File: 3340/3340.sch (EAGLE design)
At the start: 74 parts, among them IC2 CEM3340, Q1 2N3906, X1 2516-

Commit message: fixed the levels for the 3340 and vcf3
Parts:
- C6: value 1n -> 68p
- R30, R31: value 1k -> 100k
- R7, R8: value 22k -> 1k
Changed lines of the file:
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@@
 <part name="PWM" library="dan" deviceset="PJ301BM" device=""/>
 <part name="GND4" library="dan" deviceset="GND" device=""/>
-<part name="R8" library="dan" deviceset="R-US_" device="0207/7" value="22k"/>
+<part name="R8" library="dan" deviceset="R-US_" device="0207/7" value="1k"/>
 <part name="GND20" library="dan" deviceset="GND" device=""/>
 <part name="GND21" library="dan" deviceset="GND" device=""/>
@@
 <part name="C1" library="dan" deviceset="C-US" device="050-025X075" value="1n"/>
 <part name="GND5" library="dan" deviceset="GND" device=""/>
-<part name="R7" library="dan" deviceset="R-US_" device="0207/7" value="22k"/>
+<part name="R7" library="dan" deviceset="R-US_" device="0207/7" value="1k"/>
 <part name="HF" library="dan" deviceset="TRIM_US-" device="S64W" value="20k"/>
 <part name="GND11" library="dan" deviceset="GND" device=""/>
@@
 <part name="SYNC" library="dan" deviceset="PJ301BM" device=""/>
 <part name="GND6" library="dan" deviceset="GND" device=""/>
-<part name="C6" library="dan" deviceset="C-US" device="050-025X075" value="1n"/>
+<part name="C6" library="dan" deviceset="C-US" device="050-025X075" value="68p"/>
 <part name="GND9" library="dan" deviceset="GND" device=""/>
 <part name="P+4" library="dan" deviceset="+12V" device=""/>
@@
 <part name="P+6" library="dan" deviceset="+12V" device=""/>
 <part name="R29" library="dan" deviceset="R-US_" device="0207/7" value="10k"/>
-<part name="R30" library="dan" deviceset="R-US_" device="0207/7" value="1k"/>
-<part name="R31" library="dan" deviceset="R-US_" device="0207/7" value="1k"/>
+<part name="R30" library="dan" deviceset="R-US_" device="0207/7" value="100k"/>
+<part name="R31" library="dan" deviceset="R-US_" device="0207/7" value="100k"/>
 <part name="GND27" library="dan" deviceset="GND" device=""/>
 <part name="GND28" library="dan" deviceset="GND" device=""/>

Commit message: added state variable filter, changed pw resistor on vco
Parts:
- R29: value 10k -> 1k
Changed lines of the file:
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@@
 <part name="R28" library="dan" deviceset="R-US_" device="0207/7" value="10k"/>
 <part name="P+6" library="dan" deviceset="+12V" device=""/>
-<part name="R29" library="dan" deviceset="R-US_" device="0207/7" value="10k"/>
+<part name="R29" library="dan" deviceset="R-US_" device="0207/7" value="1k"/>
 <part name="R30" library="dan" deviceset="R-US_" device="0207/7" value="100k"/>
 <part name="R31" library="dan" deviceset="R-US_" device="0207/7" value="100k"/>

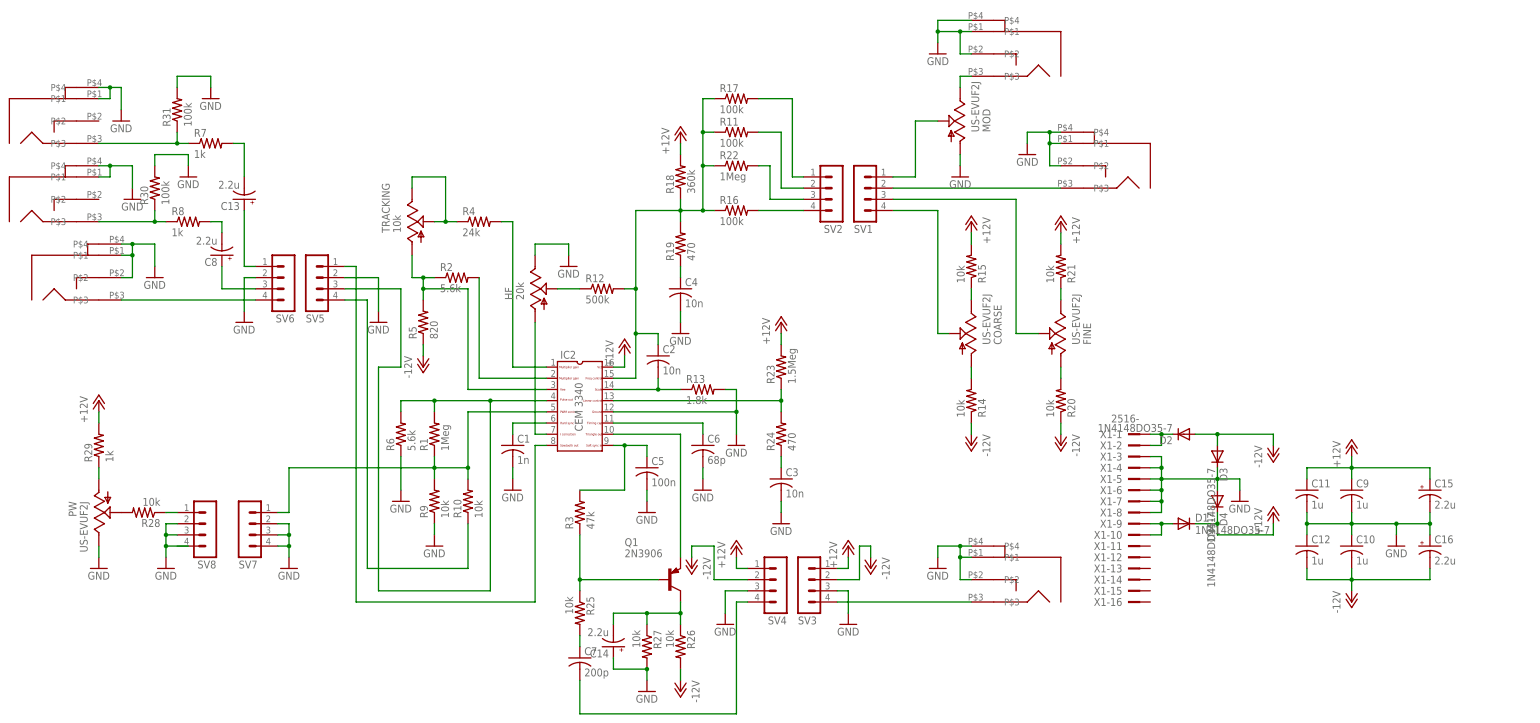
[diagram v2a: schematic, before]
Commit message: added tri and linear mod to vco, fixed serious errors with cvsource
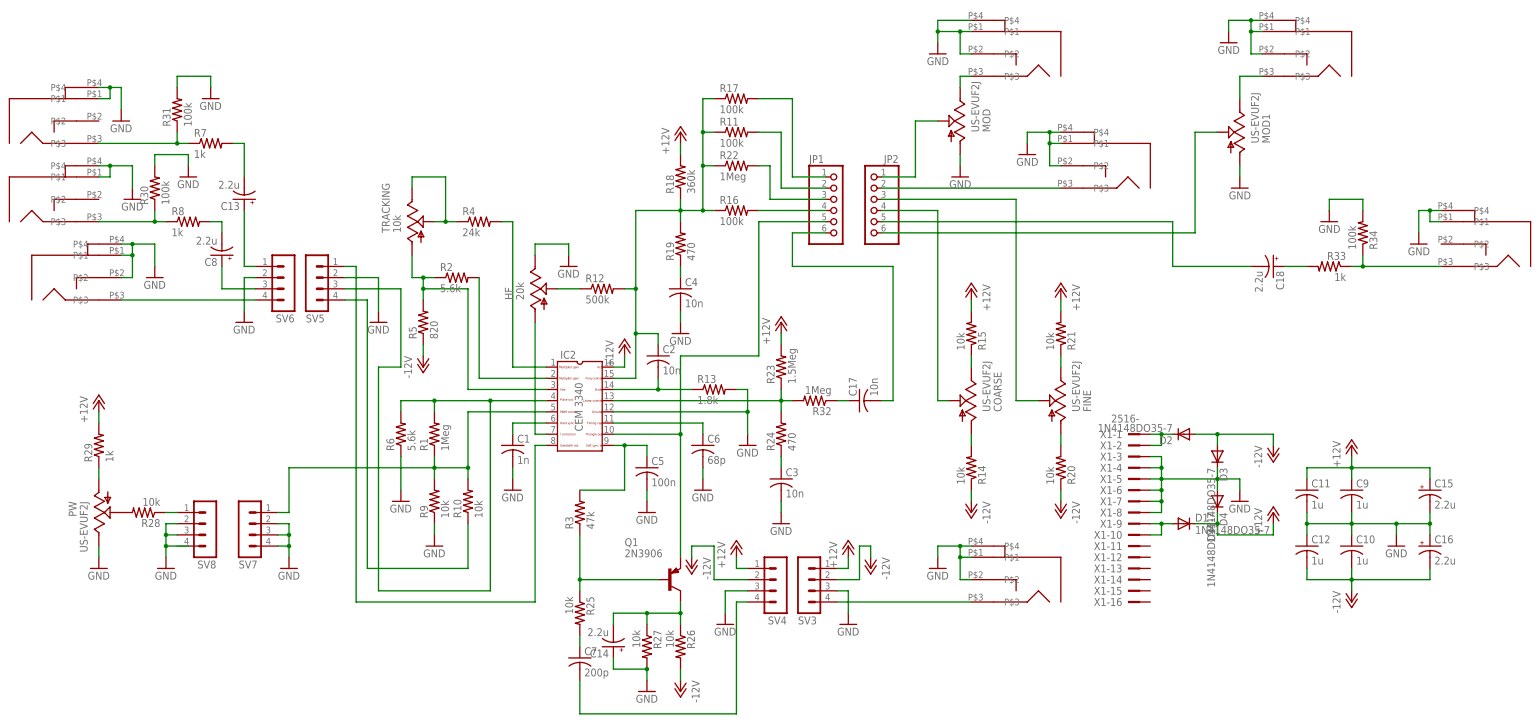
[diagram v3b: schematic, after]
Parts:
- removed SV1, SV2: (no value), dan:MA04-1
- added C17: 10n, dan:C-US050-025X075
- added C18: 2.2u, dan:CPOL-USE2.5-6
- added CVIN2, SAW1: PJ301BM, dan:PJ301BM
- added JP1, JP2: (no value), dan:PINHD-1X6
- added MOD1: US-EVUF2J, dan:US-EVUF2J
- added R32: 1Meg, dan:R-US_0207/2V
- added R33: 1k, dan:R-US_0207/7
- added R34: 100k, dan:R-US_0207/7
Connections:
- new net N$24: C17.1, R32.1
- new net N$51: C17.2, JP1.6
- new net N$52: JP2.6, MOD1.S
- new net N$53: C18.+, R33.2
- new net N$54: R33.1, R34.1, SAW1.P$3
- new net N$55: C18.-, JP2.5
- new net N$56: CVIN2.P$3, MOD1.E
- net GND: now also CVIN2.P$1, CVIN2.P$2, CVIN2.P$4, MOD1.A, R34.2, SAW1.P$1, SAW1.P$4
- net N$17: now also JP1.4; no longer SV2.4
- net N$21: now also JP1.1; no longer SV2.1
- net N$25: now also JP1.2; no longer SV2.2
- net N$31: now also JP2.1; no longer SV1.1
- net N$32: now also JP1.5
- net N$35: now also JP2.2; no longer SV1.2
- net N$37: now also JP2.3; no longer SV1.3
- net N$38: now also R32.2
- net N$39: now also JP1.3; no longer SV2.3
- net N$5: now also JP2.4; no longer SV1.4
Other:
- moved on the sheet: COARSE, FINE, R13, R14, R15, R20, R21
